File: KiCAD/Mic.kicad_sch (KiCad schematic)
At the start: 2 parts

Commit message: Set up and exported the BOM
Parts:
- MK1, R40: now left out of the parts list
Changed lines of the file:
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@@
 		(body_style 1)
 		(exclude_from_sim no)
-		(in_bom yes)
+		(in_bom no)
 		(on_board yes)
 		(in_pos_files yes)
@@
 		)
 		(property "BOM" "Yes"
+			(at 149.86 99.06 0)
+			(hide yes)
+			(show_name no)
+			(do_not_autoplace no)
+			(effects
+				(font
+					(size 1.27 1.27)
+				)
+			)
+		)
+		(property "ManPartNo" ""
 			(at 149.86 99.06 0)
 			(hide yes)
@@
 		(body_style 1)
 		(exclude_from_sim no)
-		(in_bom yes)
+		(in_bom no)
 		(on_board yes)
 		(in_pos_files yes)
@@
 			)
 		)
+		(property "ManPartNo" ""
+			(at 152.4 91.44 0)
+			(hide yes)
+			(show_name no)
+			(do_not_autoplace no)
+			(effects
+				(font
+					(size 1.27 1.27)
+				)
+			)
+		)

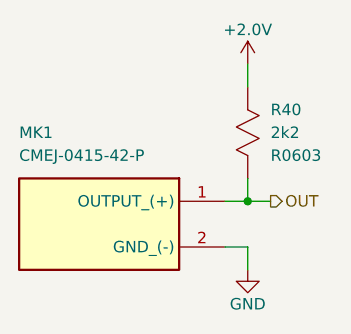
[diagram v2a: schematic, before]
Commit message: Added PA_Enable pull-down and moved the debug header
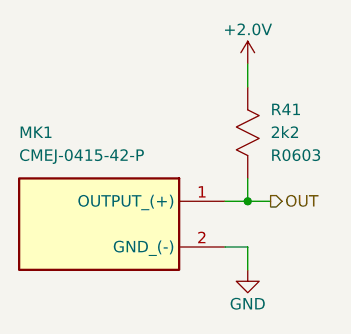
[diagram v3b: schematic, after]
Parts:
- renumbered R40 to R41
